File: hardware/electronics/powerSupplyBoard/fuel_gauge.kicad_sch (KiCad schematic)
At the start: 21 parts, among them J7 VAL, Q4 BSS84, Q5 2N7002, Q6 2N7002, U3 BQ34Z100-R2

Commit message: added footprint for 2N7002
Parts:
- Q4, Q5, Q6: footprint (none) -> DS-Package-SO:SOT23-3P95_290X130L43X40N
- U3: footprint (none) -> DS-Package-SO:TSSOP14P65_500x640X120L150X45N
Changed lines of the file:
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@@
 			)
 		)
-		(property "Footprint" ""
+		(property "Footprint" "DS-Package-SO:SOT23-3P95_290X130L43X40N"
 			(at 106.045 115.57 90)
 			(effects
@@
 			)
 		)
-		(property "Footprint" ""
+		(property "Footprint" "DS-Package-SO:SOT23-3P95_290X130L43X40N"
 			(at 117.475 90.17 90)
 			(effects
@@
 			)
 		)
-		(property "Footprint" ""
+		(property "Footprint" "DS-Package-SO:SOT23-3P95_290X130L43X40N"
 			(at 95.25 82.55 0)
 			(effects
@@
 			)
 		)
-		(property "Footprint" ""
+		(property "Footprint" "DS-Package-SO:TSSOP14P65_500x640X120L150X45N"
 			(at 139.7 107.95 0)
 			(effects

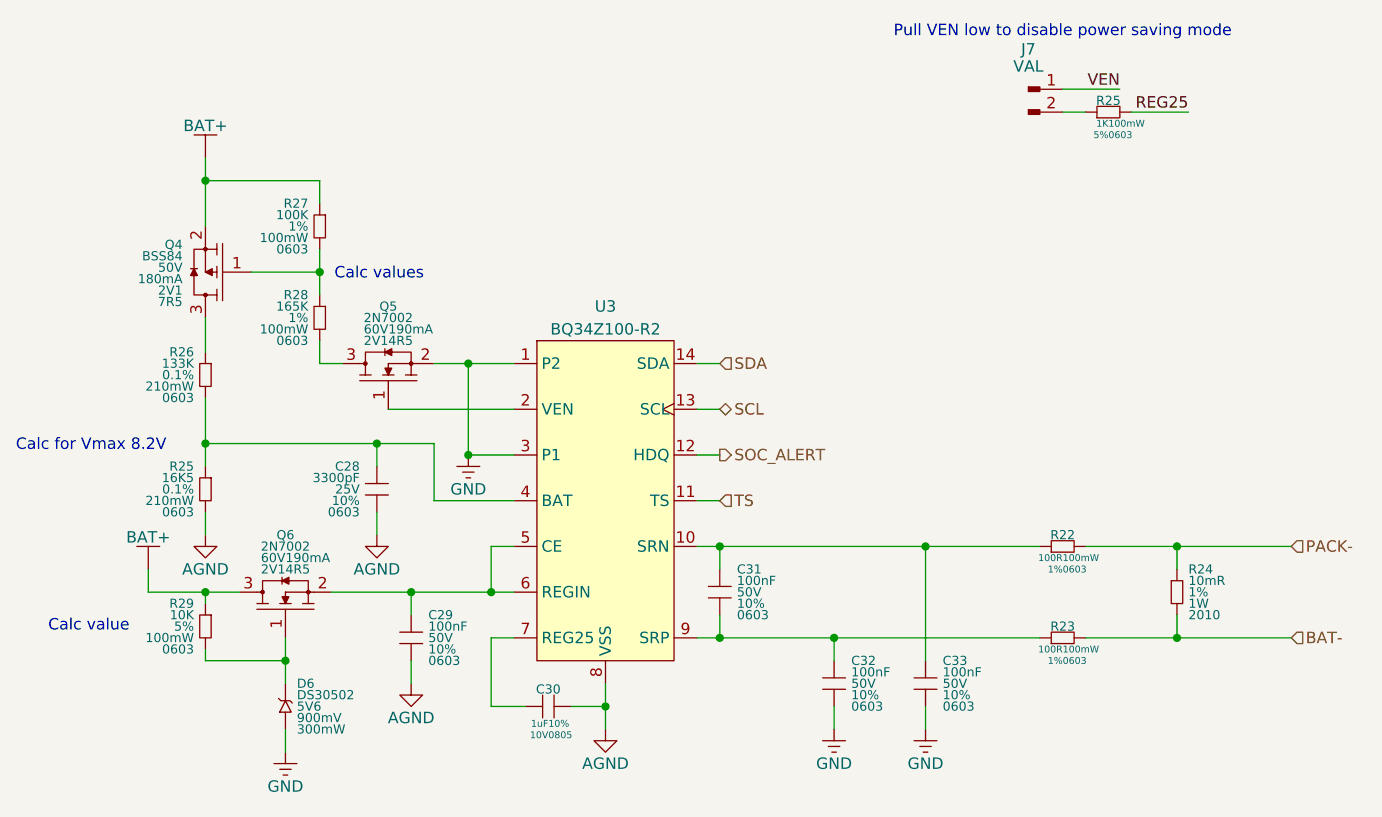
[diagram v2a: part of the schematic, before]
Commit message: renumbers passives and cleaned up sheets
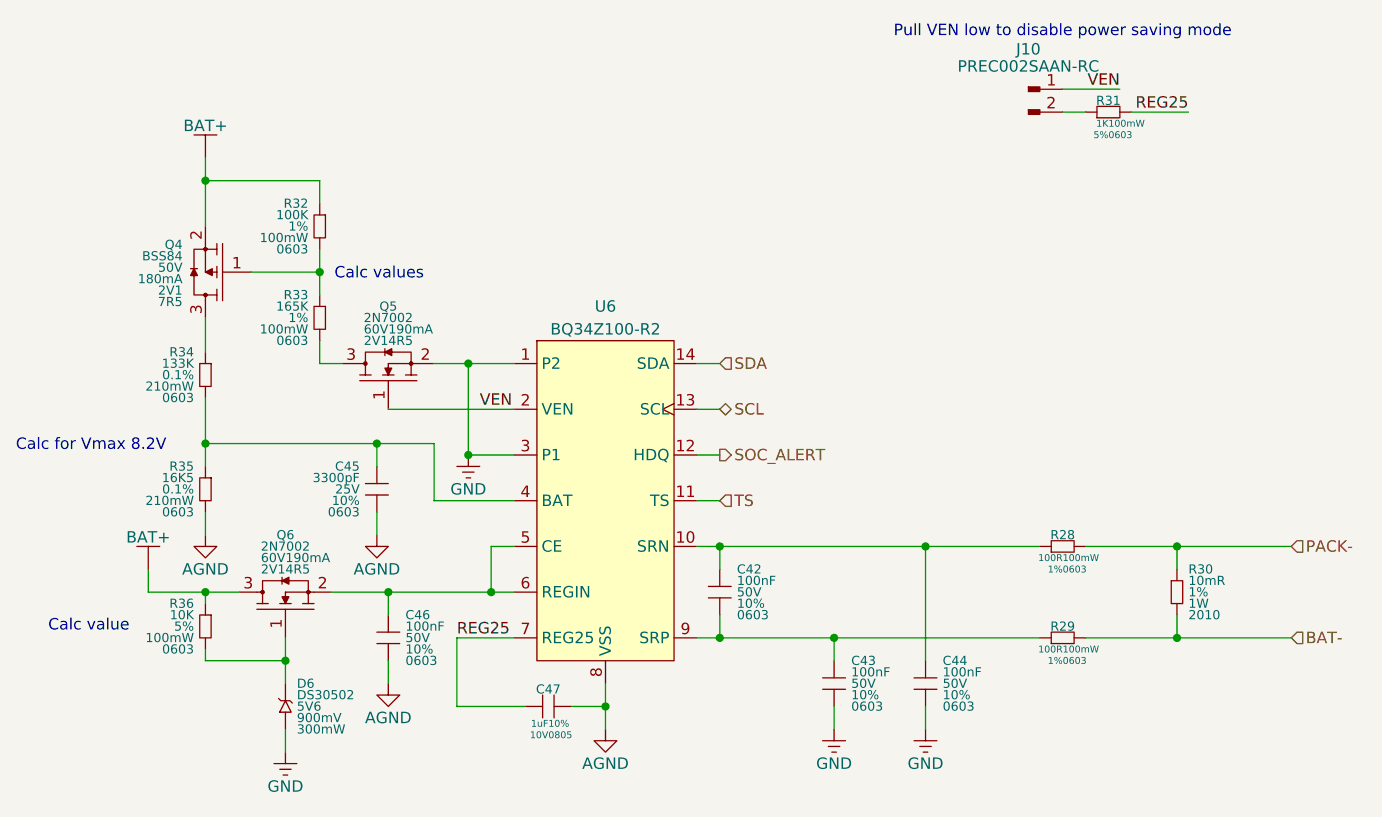
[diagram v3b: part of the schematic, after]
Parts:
- removed J7: VAL, symbol DS-Connectors:Conn_01x02_Pin
- removed R24: 10mR, DS-Resistors-SMD:WSLHP2010, symbol DSE-Passives:R
- removed R25: 16K5, DS-Resistors-SMD:CRCW0603, symbol DSE-Passives:R
- removed R26: 133K, DS-Resistors-SMD:CRCW0603, symbol DSE-Passives:R
- removed R28: 165K, DS-Resistors-SMD:CRCW0603, symbol DSE-Passives:R
- removed U3: BQ34Z100-R2, DS-Package-SO:TSSOP14P65_500x640X120L150X45N, symbol DSE-PMIC:BQ34Z100-R2
- added J10: PREC002SAAN-RC, DS-Rectangular-Connectors:conn_01x02_254, symbol lib_sch:Conn_01x02_Pin
- added R30: 10mR, DS-Resistors-SMD:WSLHP2010, symbol lib_sch:R
- added R33: 165K, DS-Resistors-SMD:CRCW0603, symbol lib_sch:R
- added R34: 133K, DS-Resistors-SMD:CRCW0603, symbol lib_sch:R
- added R35: 16K5, DS-Resistors-SMD:CRCW0603, symbol lib_sch:R
- added U6: BQ34Z100-R2, DS-Package-SO:TSSOP14P65_500x640X120L150X45N, symbol lib_sch:BQ34Z100-R2
- C42: renamed from C31; symbol DS-Passives:C -> lib_sch:C_2
- C43: renamed from C32; symbol DS-Passives:C -> lib_sch:C_2
- C44: renamed from C33; symbol DS-Passives:C -> lib_sch:C_2
- C45: renamed from C28; symbol DS-Passives:C -> lib_sch:C_2
- C46: renamed from C29; symbol DS-Passives:C -> lib_sch:C_2
- C47: renamed from C30; symbol DS-Passives:C_horizontal -> lib_sch:C_horizontal
- D6: footprint (none) -> DS-Package-SO:SOD523; symbol DS-Passives:D_Zener -> lib_sch:D_Zener
- Q4: symbol DS-Transistors:PMOS_GSD -> lib_sch:PMOS_GSD
- Q5, Q6: symbol DS-Transistors:NMOS_GSD -> lib_sch:NMOS_GSD
- R28: renamed from R22; symbol DS-Passives:R_horizontal -> lib_sch:R_horizontal
- R29: renamed from R23; symbol DS-Passives:R_horizontal -> lib_sch:R_horizontal
- R31: renamed from R25; symbol DS-Passives:R_horizontal -> lib_sch:R_horizontal
- R32: renamed from R27; symbol DS-Passives:R -> lib_sch:R
- R36: renamed from R29; symbol DS-Passives:R -> lib_sch:R
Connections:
- net AGND: now also R35.2, U6.8 (VSS)
- net BAT-: now also R30.2
- net GND: now also U6.1 (P2), U6.3 (P1)
- net PACK-: now also R30.1
- net REG25: now also C47.1, U6.7 (REG25)
- net SCL: now also U6.13 (SCL)
- net SDA: now also U6.14 (SDA)
- net SOC_ALERT: now also U6.12 (HDQ)
- net TS: now also U6.11 (TS)
- net VEN: now also Q5.1, J10.1, U6.2 (VEN)
- net at Q4.1, R32.2: now also R33.1
- net at Q5.3: now also R33.2
- net at C46.1, Q6.2: now also U6.5 (CE), U6.6 (REGIN)
- net at C42.2, C43.1, R29.1: now also U6.9 (SRP)
- net at R31.1: now also J10.2
- net at Q4.3: now also R34.1
- net at C45.1: now also R34.2, R35.1, U6.4 (BAT)
- net at C42.1, C44.1, R28.1: now also U6.10 (SRN)
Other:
- moved on the sheet: C46

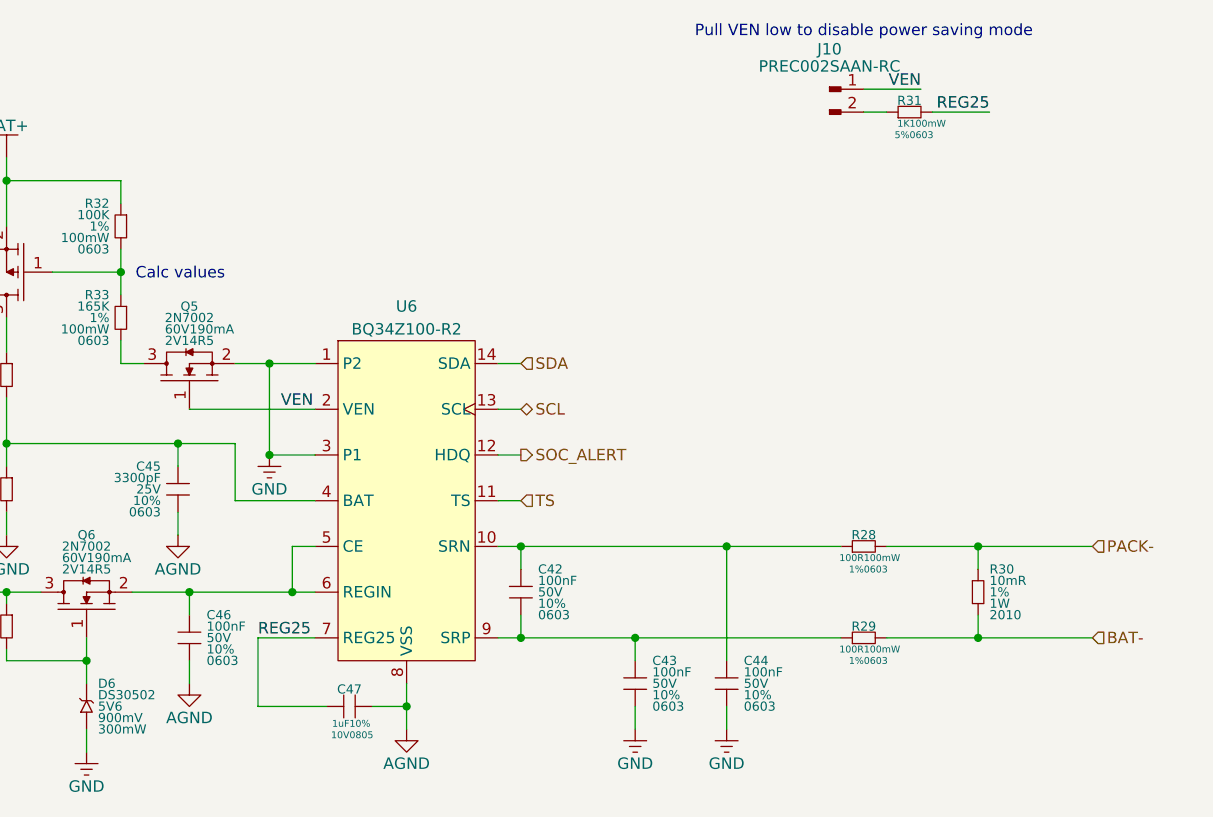
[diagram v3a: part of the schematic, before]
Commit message: fixed schematic, organized page, and fixed ground nets
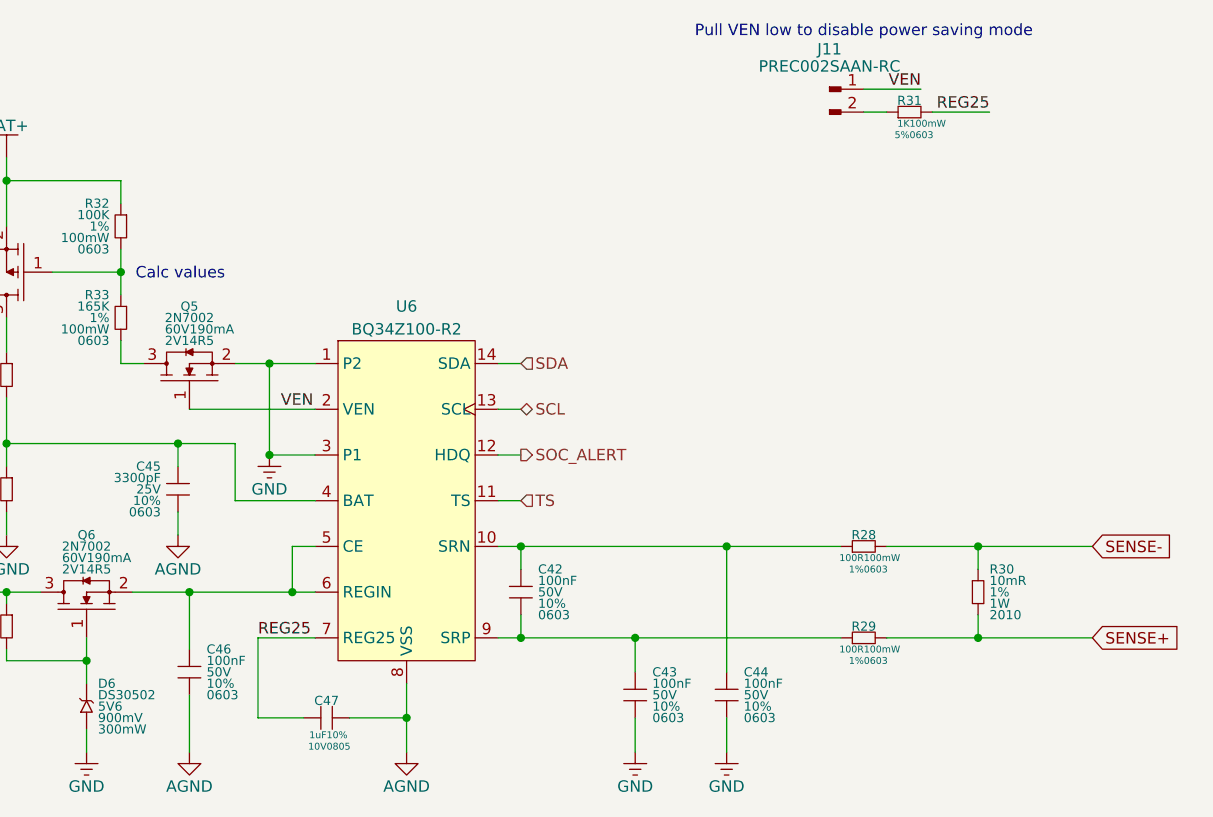
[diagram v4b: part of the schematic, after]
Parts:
- renumbered J10 to J11
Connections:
- net BAT- renamed SENSE+
- net PACK- renamed SENSE-
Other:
- moved on the sheet: C43, C44, C46, C47

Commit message: removed Rsense
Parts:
- removed R30: 10mR, DS-Resistors-SMD:WSLHP2010, symbol lib_sch:R
- renumbered R31 to R30, R32 to R31, R33 to R32, R34 to R33, R35 to R34, R36 to R35
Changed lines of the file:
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@@
 	)
 	(junction
-		(at 203.2 123.19)
-		(diameter 0)
-		(color 0 0 0 0)
-	)
-	(junction
 		(at 107.95 82.55)
 		(diameter 0)
@@
 	)
 	(junction
-		(at 203.2 113.03)
-		(diameter 0)
-		(color 0 0 0 0)
-	)
-	(junction
 		(at 139.7 132.08)
 		(diameter 0)
@@
 	(wire
 		(pts
-			(xy 203.2 123.19) (xy 215.9 123.19)
+			(xy 193.04 123.19) (xy 203.2 123.19)
 		)
 		(stroke
@@
 	(wire
 		(pts
-			(xy 193.04 123.19) (xy 203.2 123.19)
-		)
-		(stroke
-			(width 0)
-			(type default)
-		)
-	)
-	(wire
-		(pts
 			(xy 95.25 124.46) (xy 95.25 125.73)
 		)
@@
 	(wire
 		(pts
-			(xy 203.2 115.57) (xy 203.2 113.03)
-		)
-		(stroke
-			(width 0)
-			(type default)
-		)
-	)
-	(wire
-		(pts
 			(xy 95.25 118.11) (xy 95.25 119.38)
 		)
@@
 	(wire
 		(pts
-			(xy 193.04 113.03) (xy 203.2 113.03)
-		)
-		(stroke
-			(width 0)
-			(type default)
-		)
-	)
-	(wire
-		(pts
-			(xy 203.2 123.19) (xy 203.2 120.65)
-		)
-		(stroke
-			(width 0)
-			(type default)
-		)
-	)
-	(wire
-		(pts
 			(xy 99.06 118.11) (xy 95.25 118.11)
 		)
@@
 	(wire
 		(pts
-			(xy 203.2 113.03) (xy 215.9 113.03)
+			(xy 193.04 113.03) (xy 203.2 113.03)
 		)
 		(stroke
@@
 		)
 	)
+	(text_box "Vsense=Rsense*Imax\nVsense= +/-125mV\nImax ~= 4A"
+		(exclude_from_sim no)
+		(at 190.5 96.52 0)
+		(size 22.86 7.62)
+		(stroke
+			(width 0)
+			(type default)
+		)
+		(fill
+			(type none)
+		)
+		(effects
+			(font
+				(size 1.27 1.27)
+			)
+			(justify left top)
+		)
+	)
 	(text "Calc for Vmax 8.2V"
 		(exclude_from_sim no)
@@
 	(global_label "SENSE-"
 		(shape input)
-		(at 215.9 113.03 0)
+		(at 203.2 113.03 0)
 		(fields_autoplaced yes)
 		(effects
@@
 		)
 		(property "Intersheetrefs" "${INTERSHEET_REFS}"
-			(at 226.5051 113.03 0)
+			(at 213.8051 113.03 0)
 			(effects
 				(font
@@
 	(global_label "SENSE+"
 		(shape input)
-		(at 215.9 123.19 0)
+		(at 203.2 123.19 0)
 		(fields_autoplaced yes)
 		(effects
@@
 		)
 		(property "Intersheetrefs" "${INTERSHEET_REFS}"
-			(at 226.5051 123.19 0)
+			(at 213.8051 123.19 0)
 			(effects
 				(font
@@
 	)
 	(symbol
-		(lib_id "lib_sch:R")
-		(at 203.2 118.11 0)
-		(unit 1)
-		(exclude_from_sim no)
-		(in_bom yes)
-		(on_board yes)
-		(dnp no)
-		(property "Reference" "R30"
-			(at 204.47 115.57 0)
-			(do_not_autoplace yes)
-			(effects
-				(font
-					(size 1.016 1.016)
-				)
-				(justify left)
-			)
-		)
-		(property "Value" "10mR"
-			(at 204.47 116.84 0)
-			(do_not_autoplace yes)
-			(effects
-				(font
-					(size 1.016 1.016)
-				)
-				(justify left)
-			)
-		)
-		(property "Footprint" "DS-Resistors-SMD:WSLHP2010"
-			(at 203.2 115.57 0)
-			(effects
-				(font
-					(size 1.27 1.27)
-				)
-				(hide yes)
-			)
-		)
-		(property "Datasheet" "datasheets/Vishay-Dale-WSL-HP.pdf"
-			(at 203.2 115.57 0)
-			(effects
-				(font
-					(size 1.27 1.27)
-				)
-				(hide yes)
-			)
-		)
-		(property "Description" "RES 0.01 OHM 1% 1W 2010"
-			(at 203.2 118.11 0)
-			(effects
-				(font
-					(size 1.27 1.27)
-				)
-				(hide yes)
-			)
-		)
-		(property "Manufacturer" "Vishay Dale"
-			(at 203.2 115.57 0)
-			(effects
-				(font
-					(size 1.27 1.27)
-				)
-				(hide yes)
-			)
-		)
-		(property "MPN" "WSL2010R0100FEA18"
-			(at 203.2 115.57 0)
-			(effects
-				(font
-					(size 1.27 1.27)
-				)
-				(hide yes)
-			)
-		)
-		(property "DKPN" "WSLF-.01CT-ND"
-			(at 203.2 118.11 0)
-			(effects
-				(font
-					(size 1.27 1.27)
-				)
-				(hide yes)
-			)
-		)
-		(property "Tolerance" "1%"
-			(at 204.47 118.11 0)
-			(do_not_autoplace yes)
-			(effects
-				(font
-					(size 1.016 1.016)
-				)
-				(justify left)
-			)
-		)
-		(property "Power Rating" "1W"
-			(at 204.47 119.38 0)
-			(do_not_autoplace yes)
-			(effects
-				(font
-					(size 1.016 1.016)
-				)
-				(justify left)
-			)
-		)
-		(property "Package" "2010"
-			(at 204.47 120.65 0)
-			(do_not_autoplace yes)
-			(effects
-				(font
-					(size 1.016 1.016)
-				)
-				(justify left)
-			)
-		)
-		(pin "1"
-		)
-		(pin "2"
-		)
-		(instances
-			(project "powerSupplyBoard"
-				(path "/6f3ae1d2-e925-4178-b812-ea14ec542b6c/66c48dda-9393-435e-81e7-77c90d57b98a"
-					(reference "R30")
-					(unit 1)
-				)
-			)
-		)
-	)
-	(symbol
 		(lib_id "lib_sch:NMOS_GSD")
 		(at 104.14 118.11 0)
@@
 		(dnp no)
 		(fields_autoplaced yes)
-		(property "Reference" "R31"
+		(property "Reference" "R30"
 			(at 195.58 63.5 0)
 			(do_not_autoplace yes)
@@
 			(project "powerSupplyBoard"
 				(path "/6f3ae1d2-e925-4178-b812-ea14ec542b6c/66c48dda-9393-435e-81e7-77c90d57b98a"
-					(reference "R31")
+					(reference "R30")
 					(unit 1)
 				)
@@
 		(on_board yes)
 		(dnp no)
-		(property "Reference" "R32"
+		(property "Reference" "R31"
 			(at 106.68 74.93 0)
 			(do_not_autoplace yes)
@@
 			(project "powerSupplyBoard"
 				(path "/6f3ae1d2-e925-4178-b812-ea14ec542b6c/66c48dda-9393-435e-81e7-77c90d57b98a"
-					(reference "R32")
+					(reference "R31")
 					(unit 1)
 				)
@@
 		(dnp no)
 		(fields_autoplaced yes)
-		(property "Reference" "R35"
+		(property "Reference" "R34"
 			(at 93.98 104.14 0)
 			(do_not_autoplace yes)
@@
 			(project "powerSupplyBoard"
 				(path "/6f3ae1d2-e925-4178-b812-ea14ec542b6c/66c48dda-9393-435e-81e7-77c90d57b98a"
-					(reference "R35")
+					(reference "R34")
 					(unit 1)
 				)
@@
 		(dnp no)
 		(fields_autoplaced yes)
-		(property "Reference" "R34"
+		(property "Reference" "R33"
 			(at 93.98 91.44 0)
 			(do_not_autoplace yes)
@@
 			(project "powerSupplyBoard"
 				(path "/6f3ae1d2-e925-4178-b812-ea14ec542b6c/66c48dda-9393-435e-81e7-77c90d57b98a"
-					(reference "R34")
+					(reference "R33")
 					(unit 1)
 				)
@@
 		(dnp no)
 		(fields_autoplaced yes)
-		(property "Reference" "R36"
+		(property "Reference" "R35"
 			(at 93.98 119.38 0)
 			(do_not_autoplace yes)
@@
 			(project "powerSupplyBoard"
 				(path "/6f3ae1d2-e925-4178-b812-ea14ec542b6c/66c48dda-9393-435e-81e7-77c90d57b98a"
-					(reference "R36")
+					(reference "R35")
 					(unit 1)
 				)
@@
 		(dnp no)
 		(fields_autoplaced yes)
-		(property "Reference" "R33"
+		(property "Reference" "R32"
 			(at 106.68 85.09 0)
 			(do_not_autoplace yes)
@@
 			(project "powerSupplyBoard"
 				(path "/6f3ae1d2-e925-4178-b812-ea14ec542b6c/66c48dda-9393-435e-81e7-77c90d57b98a"
-					(reference "R33")
+					(reference "R32")
 					(unit 1)
 				)
